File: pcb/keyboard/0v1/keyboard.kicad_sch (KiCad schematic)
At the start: 140 parts, among them SW1 A, SW10 A, SW11 A, SW12 A, SW13 A, SW14 A, SW15 A, SW16 A, SW17 A, SW18 A, SW19 A, SW2 A, SW20 A, SW21 A, SW22 A, SW23 A, SW24 A, SW25 A, SW26 A, SW27 A, SW28 A, SW29 A, SW3 A, SW30 A, SW31 A, SW32 A, SW33 A, SW34 A, SW35 A, SW36 A, SW37 A, SW38 A, SW39 A, SW4 A, SW40 A, SW41 A, SW42 A, SW43 A, SW44 A, SW45 A, SW46 A, SW47 A, SW48 A, SW49 A, SW5 A, SW50 A, SW51 A, SW52 A, SW53 A, SW54 A, SW55 A, SW56 A, SW57 A, SW58 A, SW59 A, SW6 A, SW60 A, SW61 A, SW62 A, SW63 A, SW7 A, SW8 A, SW9 A, U1 MDBT50Q-P1MV2, Y1 32.768

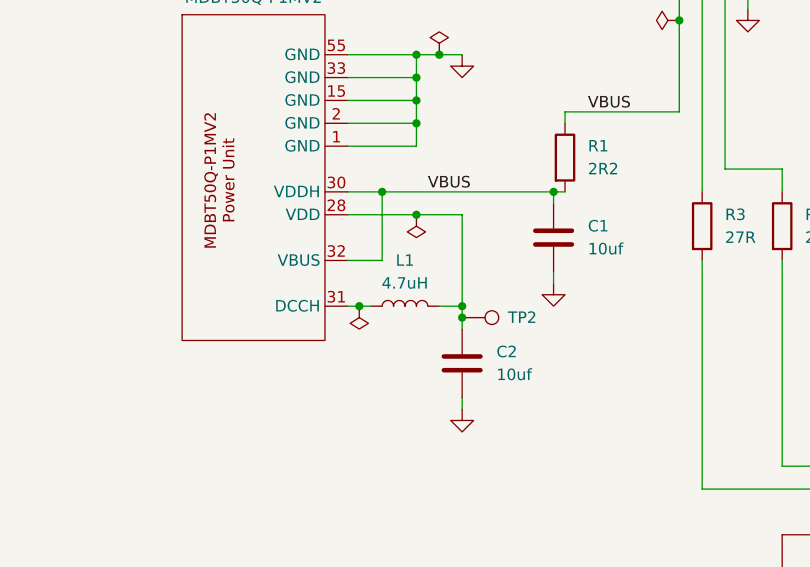
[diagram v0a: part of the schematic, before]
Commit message: Fix incorrect inductor label. 4.7uh -> 10uh
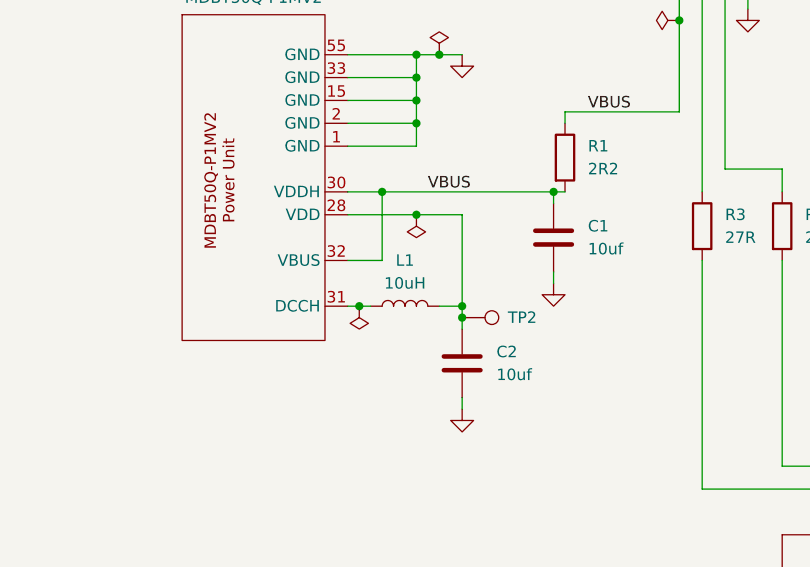
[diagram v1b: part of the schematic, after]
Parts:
- L1: value 4.7uH -> 10uH
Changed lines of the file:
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@@
 			)
 		)
-		(property "Value" "4.7uH"
+		(property "Value" "10uH"
 			(at 443.23 71.12 90)
 			(effects

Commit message: Labels :)
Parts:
- J1, J3, U1: now left out of the parts list
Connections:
- net SOURCE2: now reaches SW13.1, SW14.1, SW15.1, SW16.1, SW17.1, SW18.1, SW19.1, SW20.1, SW21.1, SW22.1, SW23.1, SW24.1, U1.20 (P0.04/AIN2)
- net SOURCE6: now reaches SW58.1, SW59.1, SW60.1, SW61.1, SW62.1, SW63.1, U1.24 (P0.08)
- net INPUT3: now reaches D15.1 (K), D2.1 (K), D27.1 (K), D39.1 (K), D51.1 (K), D59.1 (K), U1.48 (P0.24)
- net INPUT9: now reaches D21.1 (K), D33.1 (K), D45.1 (K), D54.1 (K), D62.1 (K), D9.1 (K), U1.42 (P0.19)
- net INPUT2: now reaches D1.1 (K), D14.1 (K), D26.1 (K), D38.1 (K), D50.1 (K), U1.49 (P0.25)
- net SOURCE4: now reaches SW37.1, SW38.1, SW39.1, SW40.1, SW41.1, SW42.1, SW43.1, SW44.1, SW45.1, SW46.1, SW47.1, SW48.1, U1.22 (P0.06)
- net SOURCE3: now reaches SW25.1, SW26.1, SW27.1, SW28.1, SW29.1, SW30.1, SW31.1, SW32.1, SW33.1, SW34.1, SW35.1, SW36.1, U1.21 (P0.05/AIN3)
- net INPUT1: now reaches D13.1 (K), D25.1 (K), D37.1 (K), D49.1 (K), D5.1 (K), D58.1 (K), U1.50 (P1.02)
- net INPUT4: now reaches D16.1 (K), D28.1 (K), D3.1 (K), D40.1 (K), D52.1 (K), U1.47 (P1.00/TRACEDATA0)
- net INPUT8: now reaches D20.1 (K), D32.1 (K), D44.1 (K), D8.1 (K), U1.43 (P0.21)
- net SOURCE5: now reaches SW49.1, SW50.1, SW51.1, SW52.1, SW53.1, SW54.1, SW55.1, SW56.1, SW57.1, U1.23 (P0.07/TRACECLK)
- net SOURCE1: now reaches SW1.1, SW10.1, SW11.1, SW12.1, SW2.1, SW3.1, SW4.1, SW5.1, SW6.1, SW7.1, SW8.1, SW9.1, U1.19 (P0.26)
- net INPUT12: now reaches D12.1 (K), D24.1 (K), D36.1 (K), D48.1 (K), D57.1 (K), D63.1 (K), U1.38 (P0.16)
- net INPUT11: now reaches D11.1 (K), D23.1 (K), D35.1 (K), D47.1 (K), D56.1 (K), U1.39 (P0.15)
- net INPUT6: now reaches D18.1 (K), D30.1 (K), D42.1 (K), D53.1 (K), D6.1 (K), U1.45 (PO23)
- net D-: now reaches J1.2 (D-), R3.1
- net D-: now also R3.2, U1.34 (D-)
- net D+: now reaches J1.3 (D+), R2.1
- net D+: now also R2.2, U1.35 (D+)
- net INPUT5: now reaches D17.1 (K), D29.1 (K), D4.1 (K), D41.1 (K), D60.1 (K), U1.46 (P0.22)
- net INPUT7: now reaches D19.1 (K), D31.1 (K), D43.1 (K), D61.1 (K), D7.1 (K), U1.44 (P0.20)
- net INPUT10: now reaches D10.1 (K), D22.1 (K), D34.1 (K), D46.1 (K), D55.1 (K), U1.41 (P0.17)
- net RESET: now reaches TP1.1, U1.40 (P0.18/nRESET)
- net SWDIO: now reaches J3.2 (SWDIO), U1.51 (SWDIO)
- net SWDCLK: now reaches J3.3 (SWDCLK), U1.53 (SWDCLK)
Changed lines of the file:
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@@
 		)
 	)
+	(label "INPUT8"
+		(at 476.25 135.89 180)
+		(effects
+			(font
+				(size 1.27 1.27)
+			)
+			(justify right bottom)
+		)
+	)
+	(label "D-"
+		(at 476.25 77.47 90)
+		(effects
+			(font
+				(size 1.27 1.27)
+			)
+			(justify left bottom)
+		)
+	)
+	(label "D+"
+		(at 478.79 55.88 90)
+		(effects
+			(font
+				(size 1.27 1.27)
+			)
+			(justify left bottom)
+		)
+	)
 	(label "VBUS"
 		(at 463.55 52.07 0)
@@
 		)
 	)
+	(label "INPUT11"
+		(at 476.25 146.05 180)
+		(effects
+			(font
+				(size 1.27 1.27)
+			)
+			(justify right bottom)
+		)
+	)
+	(label "D+"
+		(at 485.14 77.47 90)
+		(effects
+			(font
+				(size 1.27 1.27)
+			)
+			(justify left bottom)
+		)
+	)
+	(label "D-"
+		(at 476.25 55.88 90)
+		(effects
+			(font
+				(size 1.27 1.27)
+			)
+			(justify left bottom)
+		)
+	)
+	(label "SOURCE1"
+		(at 492.76 189.23 90)
+		(effects
+			(font
+				(size 1.27 1.27)
+			)
+			(justify left bottom)
+		)
+	)
 	(label "XL2"
 		(at 524.51 59.69 270)
@@
 		)
 	)
+	(label "INPUT6"
+		(at 476.2106 130.81 180)
+		(effects
+			(font
+				(size 1.27 1.27)
+			)
+			(justify right bottom)
+		)
+	)
+	(label "RESET"
+		(at 511.81 93.98 90)
+		(effects
+			(font
+				(size 1.27 1.27)
+			)
+			(justify left bottom)
+		)
+	)
+	(label "SOURCE4"
+		(at 500.38 189.23 90)
+		(effects
+			(font
+				(size 1.27 1.27)
+			)
+			(justify left bottom)
+		)
+	)
+	(label "INPUT7"
+		(at 476.25 133.35 180)
+		(effects
+			(font
+				(size 1.27 1.27)
+			)
+			(justify right bottom)
+		)
+	)
 	(label "VBUS"
 		(at 445.77 60.96 0)
@@
 		)
 	)
+	(label "INPUT2"
+		(at 476.25 120.65 180)
+		(effects
+			(font
+				(size 1.27 1.27)
+			)
+			(justify right bottom)
+		)
+	)
+	(label "INPUT9"
+		(at 476.25 138.43 180)
+		(effects
+			(font
+				(size 1.27 1.27)
+			)
+			(justify right bottom)
+		)
+	)
+	(label "INPUT1"
+		(at 476.25 118.11 180)
+		(effects
+			(font
+				(size 1.27 1.27)
+			)
+			(justify right bottom)
+		)
+	)
+	(label "INPUT10"
+		(at 476.25 140.97 180)
+		(effects
+			(font
+				(size 1.27 1.27)
+			)
+			(justify right bottom)
+		)
+	)
+	(label "INPUT12"
+		(at 476.25 148.59 180)
+		(effects
+			(font
+				(size 1.27 1.27)
+			)
+			(justify right bottom)
+		)
+	)
+	(label "SWDCLK"
+		(at 500.38 53.34 90)
+		(effects
+			(font
+				(size 1.27 1.27)
+			)
+			(justify left bottom)
+		)
+	)
+	(label "INPUT4"
+		(at 476.25 125.73 180)
+		(effects
+			(font
+				(size 1.27 1.27)
+			)
+			(justify right bottom)
+		)
+	)
+	(label "SWDIO"
+		(at 497.84 53.34 90)
+		(effects
+			(font
+				(size 1.27 1.27)
+			)
+			(justify left bottom)
+		)
+	)
+	(label "SOURCE6"
+		(at 505.46 189.23 90)
+		(effects
+			(font
+				(size 1.27 1.27)
+			)
+			(justify left bottom)
+		)
+	)
+	(label "SOURCE2"
+		(at 495.3 189.23 90)
+		(effects
+			(font
+				(size 1.27 1.27)
+			)
+			(justify left bottom)
+		)
+	)
+	(label "INPUT5"
+		(at 476.25 128.27 180)
+		(effects
+			(font
+				(size 1.27 1.27)
+			)
+			(justify right bottom)
+		)
+	)
 	(label "XL1"
 		(at 532.13 59.69 270)
@@
 		)
 	)
+	(label "INPUT3"
+		(at 476.25 123.19 180)
+		(effects
+			(font
+				(size 1.27 1.27)
+			)
+			(justify right bottom)
+		)
+	)
+	(label "SOURCE3"
+		(at 497.84 189.2112 90)
+		(effects
+			(font
+				(size 1.27 1.27)
+			)
+			(justify left bottom)
+		)
+	)
+	(label "SOURCE5"
+		(at 502.92 189.23 90)
+		(effects
+			(font
+				(size 1.27 1.27)
+			)
+			(justify left bottom)
+		)
+	)
 	(symbol
 		(lib_id "Switch:SW_Push_45deg")
@@
 		(unit 1)
 		(exclude_from_sim no)
-		(in_bom yes)
+		(in_bom no)
 		(on_board yes)
 		(dnp no)
@@
 		(unit 1)
 		(exclude_from_sim no)
-		(in_bom yes)
+		(in_bom no)
 		(on_board yes)
 		(dnp no)
@@
 		(unit 2)
 		(exclude_from_sim no)
-		(in_bom yes)
+		(in_bom no)
 		(on_board yes)
 		(dnp no)
@@
 		(unit 1)
 		(exclude_from_sim no)
-		(in_bom yes)
+		(in_bom no)
 		(on_board yes)
 		(dnp no)
